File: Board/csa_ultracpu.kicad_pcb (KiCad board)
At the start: 4 copper layers, 160 x 100.1 mm, 183 parts, among them IC1 74LVC125, IC13 74244DW, IC14 74LVC14, IC16 74LVC8T245SO24, IC18 74LVC06, IC19 74244DW, IC4 74HCT245DW, IC5 74HCT245DW, IC6 741G04DBV, IC7 74LVC138, IC8 MAX3421E, J1 HDMI_A, P1 CSABUS, Q2 32kHz, Q3 12MHz, U1 IS61WV51216EDALL, U2 XC6SLX25T-CSG324, U5 IS61WV51216EDALL, X1 SJ1-3513N, X3 SG-8002CE

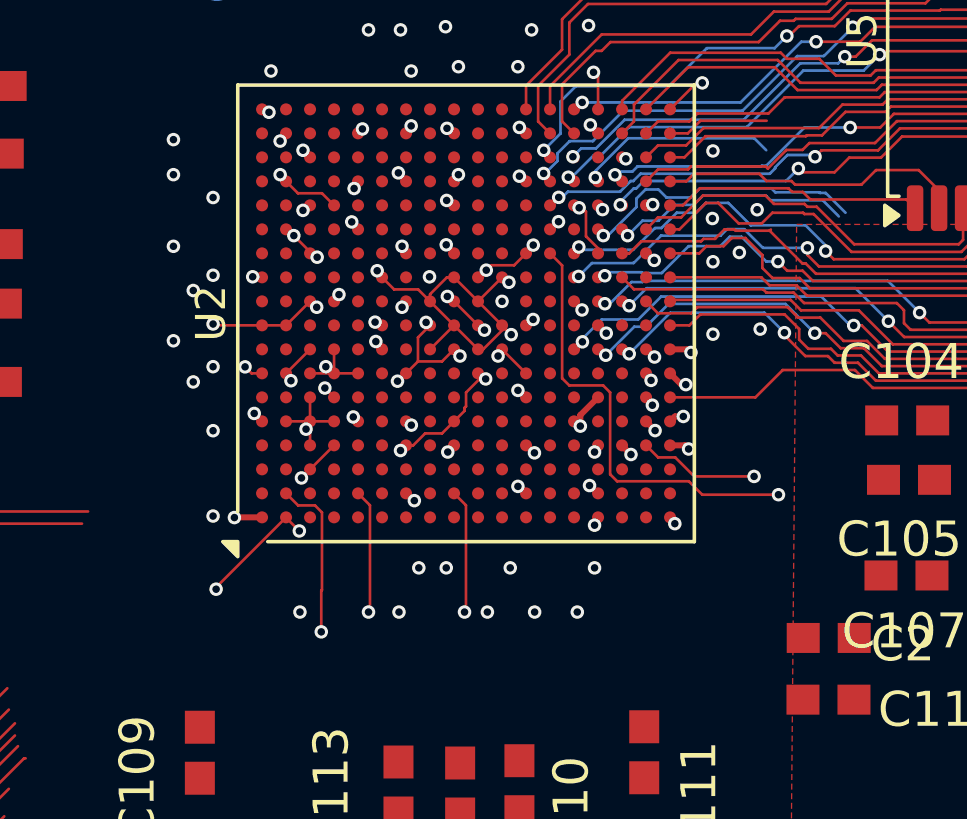
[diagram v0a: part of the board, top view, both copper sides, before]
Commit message: replace Spartan6 xc6slx25t with cheaper xc6slx65, start re-layout
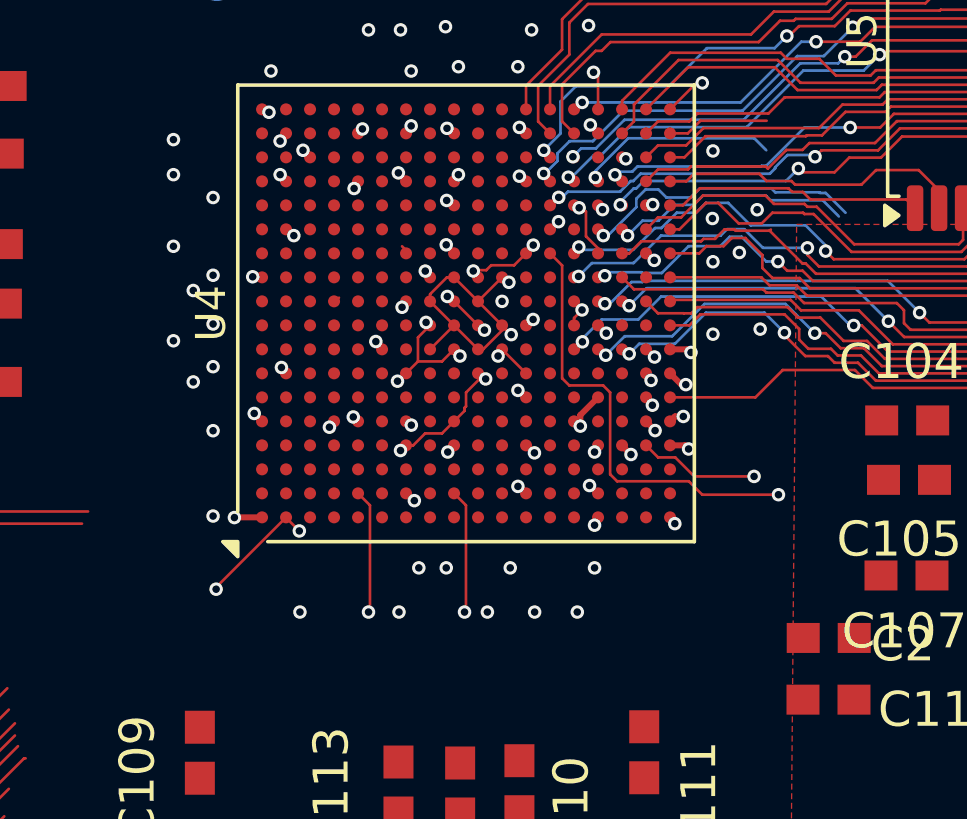
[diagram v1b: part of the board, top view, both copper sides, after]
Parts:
- removed U2: XC6SLX25T-CSG324, Package_BGA:Xilinx_CSGA324
- added U4: XC6SLX25-CSG324, Package_BGA:Xilinx_CSG324, F.Cu at (151.2, 96.2)
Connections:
- net /CPU,RAM,ROM/SPI_NFLASH renamed /SPI_FLASH
- net /CPU,RAM,ROM//FPGA_BOOT renamed /FPGA_BOOT
- IC1 pad 6: Net-(IC1B-O) -> unconnected-(IC1B-O-Pad6)
- U$4 pad 2: SPI_MISO/DIN -> unconnected-(U$4-SO-Pad2)
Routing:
- net GND: track 1028.1 -> 1008.1 mm, vias 101 -> 94
- net unconnected-(U4B-IO_L13P_M1_2-PadN12): track 0.00 -> 14.7 mm, vias 0 -> 1
- net Net-(IC1B-O): track 14.7 -> 0.00 mm, vias 1 -> 0
- net V33: track 1103.7 -> 1093.9 mm, vias 89 -> 88
- net SPI_MISO/DIN: track 148.3 -> 138.5 mm, vias 9 -> 8
- net unconnected-(U4B-IO_L3P_D0_DIN_MISO_MISO1_2-PadR13): track 0.00 -> 9.74 mm, vias 0 -> 1
- net unconnected-(U4B-IO_L3N_MOSI_CSI_B_MISO0_2-PadT13): track 0.00 -> 8.17 mm, vias 0 -> 1
- net SPI_MOSI: track 141.6 -> 133.5 mm, vias 5 -> 4
- net SPI_CLK/CCLK: track 143.1 -> 136.4 mm, vias 9 -> 8
- net unconnected-(U4B-IO_L1P_CCLK_2-PadR15): track 0.00 -> 6.71 mm, vias 0 -> 1
- net Net-(IC1A-O): track 5.45 -> 0.00 mm, vias 1 -> 0
- net V12: track 151.5 -> 147.6 mm, vias 19 -> 15

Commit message: more layout work
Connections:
- U4 pad C10: unconnected-(U4A-IO_L37P_GCLK13_0-PadC10) -> A3
- U4 pad C9: unconnected-(U4A-IO_L34N_GCLK18_0-PadC9) -> A4
- U4 pad E11: unconnected-(U4A-IO_L42N_0-PadE11) -> A1
- U4 pad F10: unconnected-(U4A-IO_L40N_0-PadF10) -> A2
- U4 pad F11: unconnected-(U4A-IO_L42P_0-PadF11) -> A0
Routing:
- net V33: track 1093.9 -> 1116.3 mm, vias 88 -> 92
- net A2: track 64.3 -> 86.1 mm, vias 4 -> 5
- net A1: track 64.1 -> 85.2 mm, vias 4 -> 5
- net A0: track 70.2 -> 90.8 mm, vias 4 -> 5
- net A3: track 95.5 -> 115.0 mm, vias 4 -> 5
- net A4: track 98.6 -> 117.7 mm, vias 4 -> 5
- net GND: track 1008.1 -> 1025.6 mm, vias 94 -> 97
- net unconnected-(U4A-IO_L38N_VREF_0-PadF9): track 0.15 -> 8.28 mm, vias 0 -> 1
- net unconnected-(U4B-IO_L55N_M3A14_3-PadF5): track 0.00 -> 8.07 mm, vias 0 -> 1
- net unconnected-(U4B-IO_L54P_M3RESET_3-PadE4): track 0.00 -> 7.81 mm, vias 0 -> 1
- net unconnected-(U4A-IO_L11P_0-PadD8): track 0.00 -> 7.25 mm, vias 0 -> 1
- net unconnected-(U4B-IO_L51P_M3A10_3-PadF4): track 0.00 -> 7.10 mm, vias 0 -> 1
- net unconnected-(U4B-IO_L54N_M3A11_3-PadD3): track 0.00 -> 6.88 mm, vias 0 -> 1
- net unconnected-(U4B-IO_L44P_GCLK21_M3A5_3-PadH4): track 0.00 -> 6.67 mm, vias 0 -> 1
- net unconnected-(U4A-IO_L3P_0-PadD6): track 0.00 -> 6.64 mm, vias 0 -> 1
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
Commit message: more layout work
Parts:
- removed IC7: 74LVC138, csa_ultracpu:SO16
- moved C109 2.06 mm to (144.0, 112.0)
- moved C111 1.17 mm to (157.1, 112.0)
- moved C110 0.06 mm to (153.0, 112.0)
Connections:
- net /CPU,RAM,ROM/E renamed E
- net /CPU,RAM,ROM/VDA renamed VDA
- net /CPU,RAM,ROM/VPB renamed VPB
- IC5 pad 15: A15 -> FA15
- IC5 pad 16: A14 -> FA14
- IC5 pad 17: A13 -> FA13
- IC5 pad 18: A12 -> FA12
- U$1 pad 8: /CPU,RAM,ROM/VPA -> VPA
- U1 pad 1: A0 -> FA12
- U1 pad 2: A1 -> FA13
- U1 pad 25: FA12 -> A0
- U1 pad 26: FA13 -> A1
- U1 pad 27: FA14 -> A2
- U1 pad 28: FA18 -> A3
- U1 pad 3: A2 -> FA14
- U1 pad 4: A3 -> FA15
- U1 pad 42: FA15 -> FA18
- U4 pad A10: unconnected-(U4A-IO_L37N_GCLK12_0-PadA10) -> /FRAMUB
- U4 pad A11: unconnected-(U4A-IO_L39N_0-PadA11) -> FA16
- U4 pad A15: unconnected-(U4A-IO_L64N_SCP4_0-PadA15) -> /RES
- U4 pad B11: unconnected-(U4A-IO_L39P_0-PadB11) -> /FRAMSEL
- U4 pad B9: unconnected-(U4A-IO_L35P_GCLK17_0-PadB9) -> /FRAMLB
- U4 pad C10: A3 -> FA15
- U4 pad C11: unconnected-(U4A-IO_L36N_GCLK14_0-PadC11) -> FA17
- U4 pad C9: A4 -> FA18
- U4 pad E11: A1 -> FA13
- U4 pad F1: unconnected-(U4B-IO_L48N_M3BA1_3-PadF1) -> A15
- U4 pad F10: A2 -> FA14
- U4 pad F11: A0 -> FA12
- U4 pad H1: unconnected-(U4B-IO_L41N_GCLK26_M3DQ5_3-PadH1) -> A14
- U4 pad H2: unconnected-(U4B-IO_L41P_GCLK27_M3DQ4_3-PadH2) -> A13
- U4 pad J1: unconnected-(U4B-IO_L40N_M3DQ7_3-PadJ1) -> A12
- U4 pad K1: unconnected-(U4B-IO_L38N_M3DQ3_3-PadK1) -> A11
- U4 pad K2: unconnected-(U4B-IO_L38P_M3DQ2_3-PadK2) -> A10
- U4 pad L1: unconnected-(U4B-IO_L37N_M3DQ1_3-PadL1) -> A9
- U4 pad L2: unconnected-(U4B-IO_L37P_M3DQ0_3-PadL2) -> A7
- U4 pad M1: unconnected-(U4B-IO_L36N_M3DQ9_3-PadM1) -> A0
- U4 pad N1: unconnected-(U4B-IO_L35N_M3DQ11_3-PadN1) -> A5
- U4 pad N2: unconnected-(U4B-IO_L35P_M3DQ10_3-PadN2) -> A3
- U4 pad N3: unconnected-(U4B-IO_L1N_VREF_3-PadN3) -> A6
- U4 pad P1: unconnected-(U4B-IO_L34N_M3UDQSN_3-PadP1) -> A4
- U4 pad P2: unconnected-(U4B-IO_L34P_M3UDQS_3-PadP2) -> A2
- U4 pad P4: unconnected-(U4B-IO_L2P_3-PadP4) -> VPA
- U4 pad T1: unconnected-(U4B-IO_L33N_M3DQ13_3-PadT1) -> A1
- U4 pad T2: unconnected-(U4B-IO_L33P_M3DQ12_3-PadT2) -> SPI_ACLK
- U4 pad U1: unconnected-(U4B-IO_L32N_M3DQ15_3-PadU1) -> SPI_NAUDIO
- U4 pad U2: unconnected-(U4B-IO_L32P_M3DQ14_3-PadU2) -> SPI_AMOSI
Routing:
- net FA15: track 10.8 -> 82.9 mm, vias 0 -> 5
- net FA14: track 14.5 -> 85.2 mm, vias 0 -> 5
- net FA13: track 14.2 -> 84.1 mm, vias 0 -> 5
- net FA12: track 14.2 -> 84.0 mm, vias 0 -> 5
- net A1: track 85.2 -> 137.5 mm, vias 5 -> 6
- net A13: track 67.1 -> 18.9 mm, vias 3 -> 0
- net A7: track 39.8 -> 85.5 mm, vias 2 -> 4
- net A5: track 44.7 -> 90.0 mm, vias 2 -> 4
- net A0: track 90.8 -> 134.5 mm, vias 5 -> 6
- net A10: track 41.7 -> 84.7 mm, vias 0 -> 3
- net A2: track 86.1 -> 128.8 mm, vias 5 -> 6
- net A9: track 40.6 -> 82.5 mm, vias 1 -> 4
- net VPA: track 0.00 -> 38.5 mm, vias 0 -> 2
- net /RES: track 280.3 -> 318.6 mm, vias 11 -> 12
- net A11: track 43.6 -> 81.3 mm, vias 2 -> 5
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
